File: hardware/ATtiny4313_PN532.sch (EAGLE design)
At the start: 21 parts, among them IC1 ATtiny4313, J2 AVR ISP, U1 PCA9543AD,118, U3 LTC490CN8PBF, U4 LTC490CN8PBF

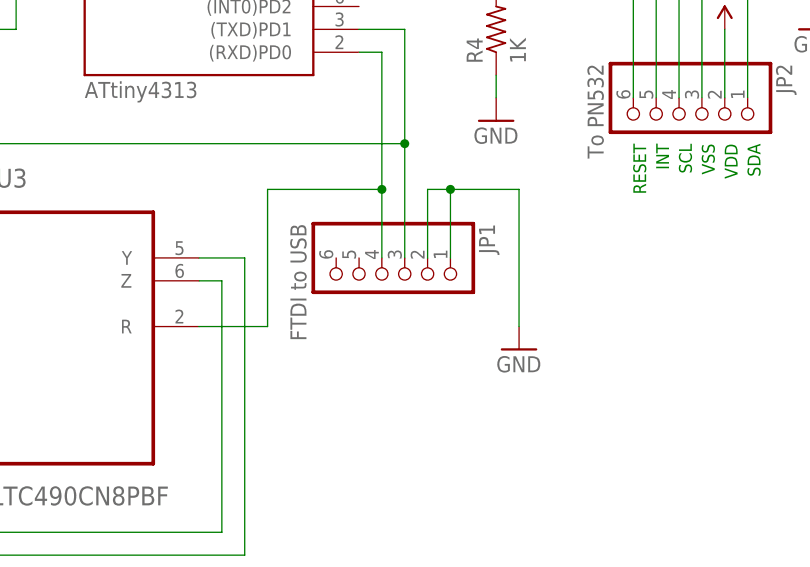
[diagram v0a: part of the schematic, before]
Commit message: Added I2C interface board (for prototypes)
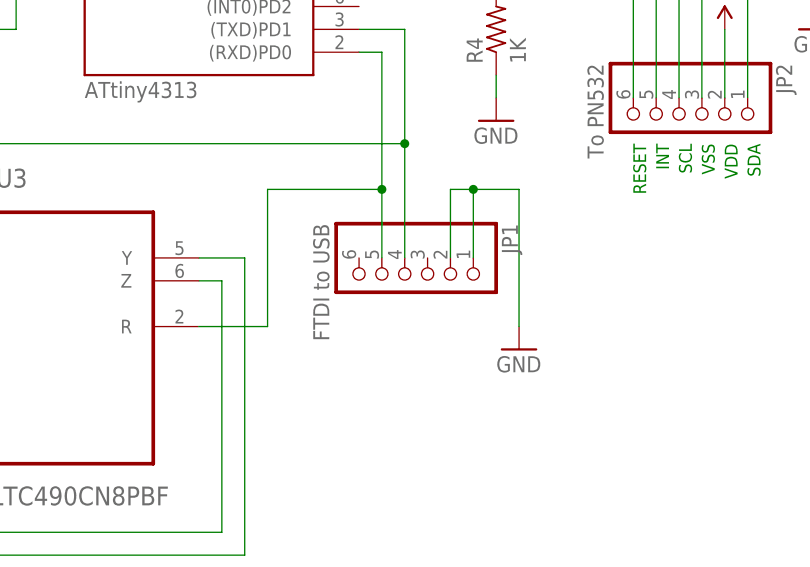
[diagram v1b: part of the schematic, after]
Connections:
- net N$3: now also JP1.4; no longer JP1.3
- net N$4: now also JP1.5; no longer JP1.4
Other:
- moved on the sheet: JP1
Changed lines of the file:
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@@
 <instance part="P+2" gate="1" x="203.2" y="175.26"/>
 <instance part="J2" gate="G$1" x="86.36" y="162.56"/>
-<instance part="JP1" gate="A" x="106.68" y="81.28" rot="R270"/>
+<instance part="JP1" gate="A" x="109.22" y="81.28" rot="R270"/>
 <instance part="GND3" gate="1" x="121.92" y="73.66"/>
 <instance part="LED1" gate="G$1" x="119.38" y="121.92"/>
@@
 <wire x1="121.92" y1="91.44" x2="121.92" y2="76.2" width="0.1524" layer="91"/>
 <pinref part="JP1" gate="A" pin="2"/>
-<wire x1="111.76" y1="83.82" x2="111.76" y2="91.44" width="0.1524" layer="91"/>
-<wire x1="111.76" y1="91.44" x2="114.3" y2="91.44" width="0.1524" layer="91"/>
+<wire x1="114.3" y1="83.82" x2="114.3" y2="91.44" width="0.1524" layer="91"/>
+<wire x1="114.3" y1="91.44" x2="116.84" y2="91.44" width="0.1524" layer="91"/>
 <pinref part="JP1" gate="A" pin="1"/>
-<wire x1="114.3" y1="91.44" x2="121.92" y2="91.44" width="0.1524" layer="91"/>
-<wire x1="114.3" y1="83.82" x2="114.3" y2="91.44" width="0.1524" layer="91"/>
-<junction x="114.3" y="91.44"/>
+<wire x1="116.84" y1="91.44" x2="121.92" y2="91.44" width="0.1524" layer="91"/>
+<wire x1="116.84" y1="83.82" x2="116.84" y2="91.44" width="0.1524" layer="91"/>
+<junction x="116.84" y="91.44"/>
 </segment>
 <segment>
@@
 <wire x1="104.14" y1="109.22" x2="109.22" y2="109.22" width="0.1524" layer="91"/>
 <wire x1="109.22" y1="109.22" x2="109.22" y2="96.52" width="0.1524" layer="91"/>
-<pinref part="JP1" gate="A" pin="3"/>
 <pinref part="U3" gate="A" pin="D"/>
-<wire x1="109.22" y1="96.52" x2="109.22" y2="83.82" width="0.1524" layer="91"/>
 <wire x1="50.8" y1="71.12" x2="45.72" y2="71.12" width="0.1524" layer="91"/>
 <wire x1="45.72" y1="71.12" x2="45.72" y2="96.52" width="0.1524" layer="91"/>
 <wire x1="45.72" y1="96.52" x2="109.22" y2="96.52" width="0.1524" layer="91"/>
+<pinref part="JP1" gate="A" pin="4"/>
+<wire x1="109.22" y1="96.52" x2="109.22" y2="83.82" width="0.1524" layer="91"/>
 <junction x="109.22" y="96.52"/>
 </segment>
@@
 <segment>
 <pinref part="IC1" gate="G$1" pin="(RXD)PD0"/>
-<pinref part="JP1" gate="A" pin="4"/>
 <wire x1="104.14" y1="106.68" x2="106.68" y2="106.68" width="0.1524" layer="91"/>
 <wire x1="106.68" y1="106.68" x2="106.68" y2="91.44" width="0.1524" layer="91"/>
 <pinref part="U3" gate="A" pin="R"/>
-<wire x1="106.68" y1="91.44" x2="106.68" y2="83.82" width="0.1524" layer="91"/>
 <wire x1="86.36" y1="76.2" x2="93.98" y2="76.2" width="0.1524" layer="91"/>
 <wire x1="93.98" y1="76.2" x2="93.98" y2="91.44" width="0.1524" layer="91"/>
 <wire x1="93.98" y1="91.44" x2="106.68" y2="91.44" width="0.1524" layer="91"/>
+<pinref part="JP1" gate="A" pin="5"/>
+<wire x1="106.68" y1="91.44" x2="106.68" y2="83.82" width="0.1524" layer="91"/>
 <junction x="106.68" y="91.44"/>
 </segment>

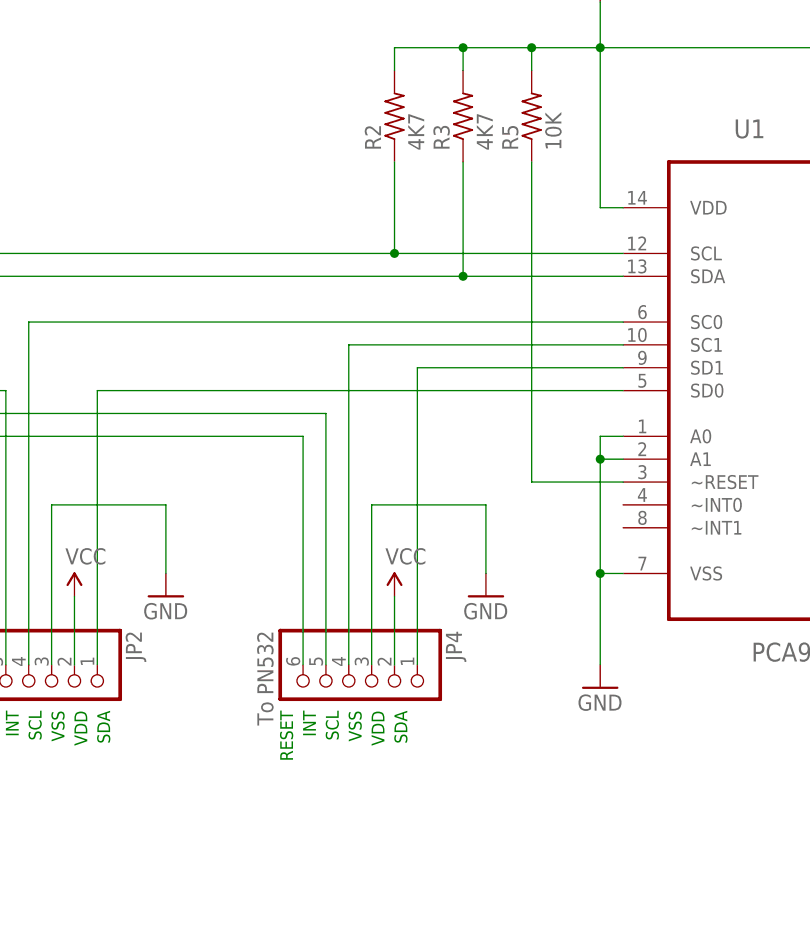
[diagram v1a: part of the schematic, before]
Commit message: Connected PCA9543 to reset to match the hardware
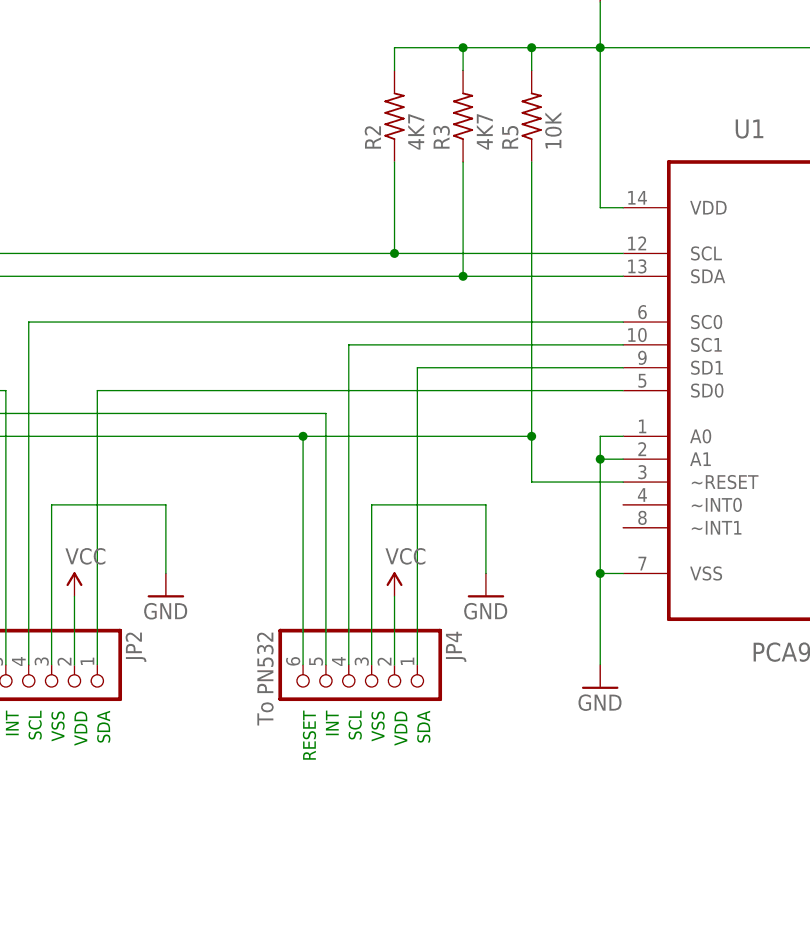
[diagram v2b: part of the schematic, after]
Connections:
- removed net N$15: R5.1, U1.~RESET
- net N$14: now also R5.1, U1.~RESET
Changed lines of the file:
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@@
 <setting verticaltext="up"/>
 </settings>
-<grid distance="0.1" unitdist="inch" unit="inch" style="lines" multiple="1" display="yes" altdistance="0.01" altunitdist="inch" altunit="inch"/>
+<grid distance="0.1" unitdist="inch" unit="inch" style="lines" multiple="1" display="no" altdistance="0.01" altunitdist="inch" altunit="inch"/>
 <layers>
 <layer number="1" name="Top" color="4" fill="1" visible="no" active="no"/>
@@
 <text x="137.16" y="96.52" size="1.4224" layer="91" rot="R270">INT</text>
 <text x="134.62" y="96.52" size="1.4224" layer="91" rot="R270">RESET</text>
-<text x="180.34" y="96.52" size="1.4224" layer="91" rot="R270">SDA</text>
-<text x="177.8" y="96.52" size="1.4224" layer="91" rot="R270">VDD</text>
-<text x="175.26" y="96.52" size="1.4224" layer="91" rot="R270">VSS</text>
-<text x="172.72" y="96.52" size="1.4224" layer="91" rot="R270">SCL</text>
-<text x="170.18" y="96.52" size="1.4224" layer="91" rot="R270">INT</text>
-<text x="167.64" y="96.52" size="1.4224" layer="91" rot="R270">RESET</text>
+<text x="182.88" y="96.52" size="1.4224" layer="91" rot="R270">SDA</text>
+<text x="180.34" y="96.52" size="1.4224" layer="91" rot="R270">VDD</text>
+<text x="177.8" y="96.52" size="1.4224" layer="91" rot="R270">VSS</text>
+<text x="175.26" y="96.52" size="1.4224" layer="91" rot="R270">SCL</text>
+<text x="172.72" y="96.52" size="1.4224" layer="91" rot="R270">INT</text>
+<text x="170.18" y="96.52" size="1.4224" layer="91" rot="R270">RESET</text>
 </plain>
 <instances>
@@
 <pinref part="JP2" gate="A" pin="6"/>
 <pinref part="JP4" gate="A" pin="6"/>
-</segment>
-</net>
-<net name="N$15" class="0">
-<segment>
 <pinref part="U1" gate="A" pin="~RESET"/>
-<wire x1="195.58" y1="157.48" x2="195.58" y2="121.92" width="0.1524" layer="91"/>
+<wire x1="195.58" y1="157.48" x2="195.58" y2="127" width="0.1524" layer="91"/>
+<wire x1="195.58" y1="127" x2="195.58" y2="121.92" width="0.1524" layer="91"/>
 <wire x1="195.58" y1="121.92" x2="205.74" y2="121.92" width="0.1524" layer="91"/>
 <pinref part="R5" gate="G$1" pin="1"/>
-</segment>
-</net>
+<wire x1="170.18" y1="127" x2="195.58" y2="127" width="0.1524" layer="91"/>
+<junction x="170.18" y="127"/>
+<junction x="195.58" y="127"/>
+</segment>
+</net>

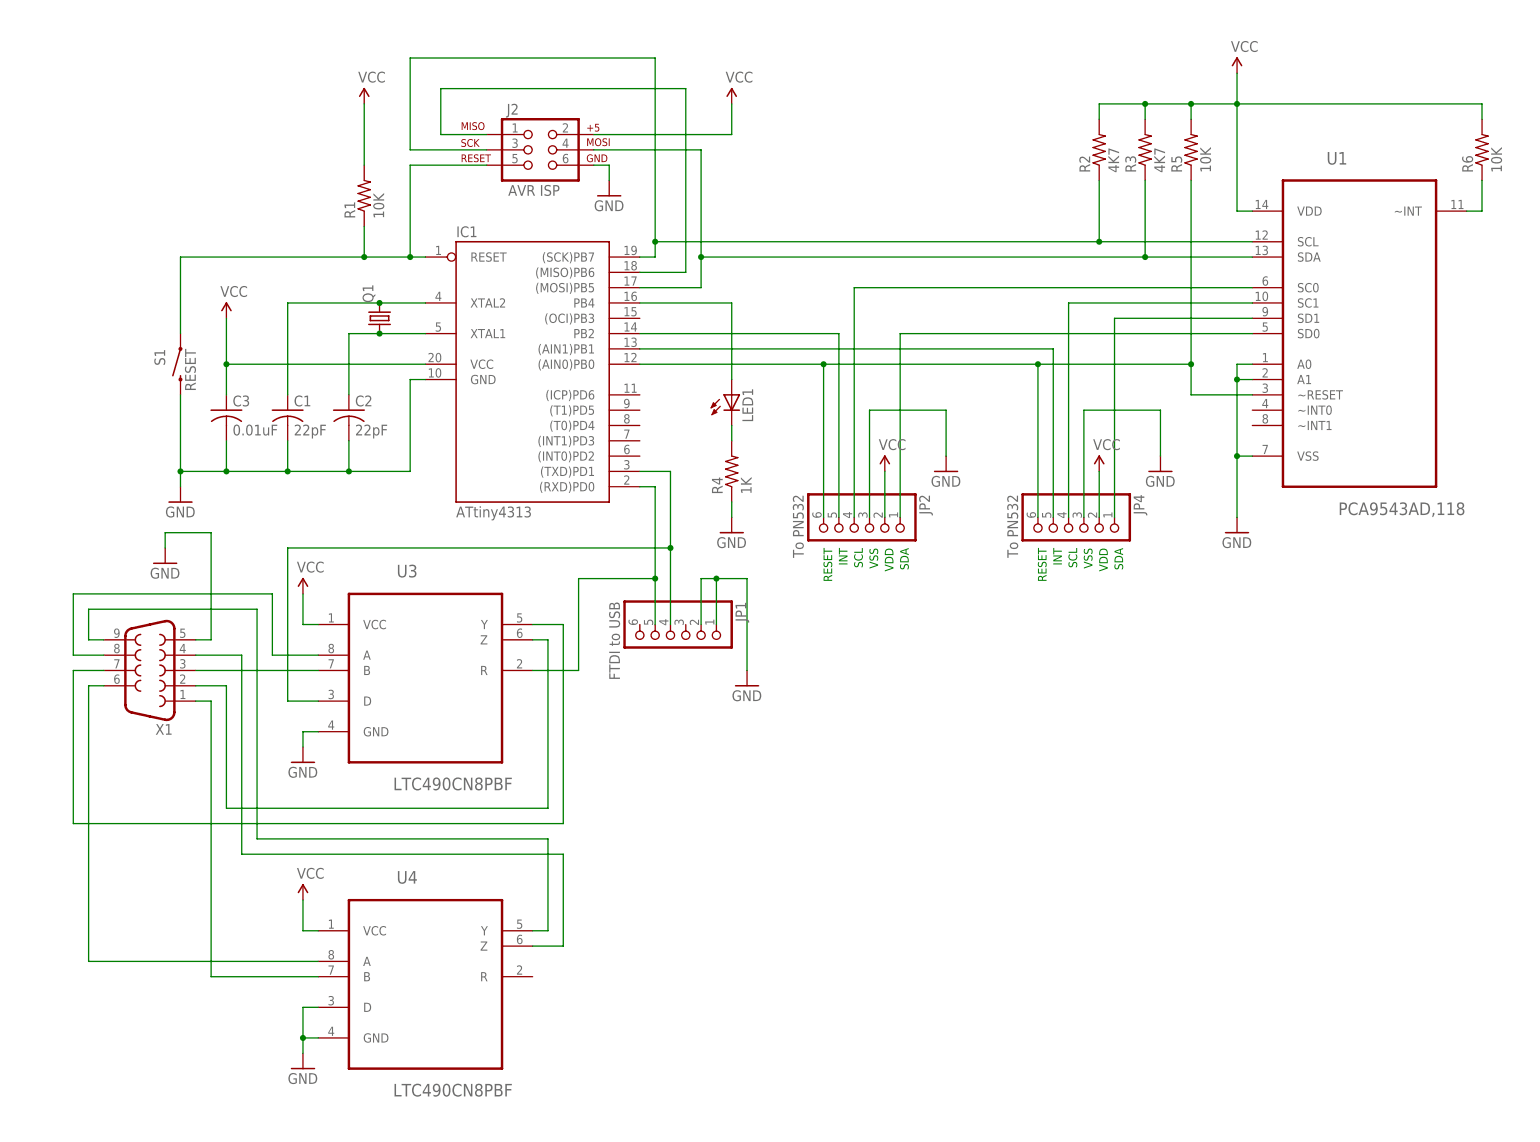
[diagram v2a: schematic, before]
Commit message: Corrected INT wiring
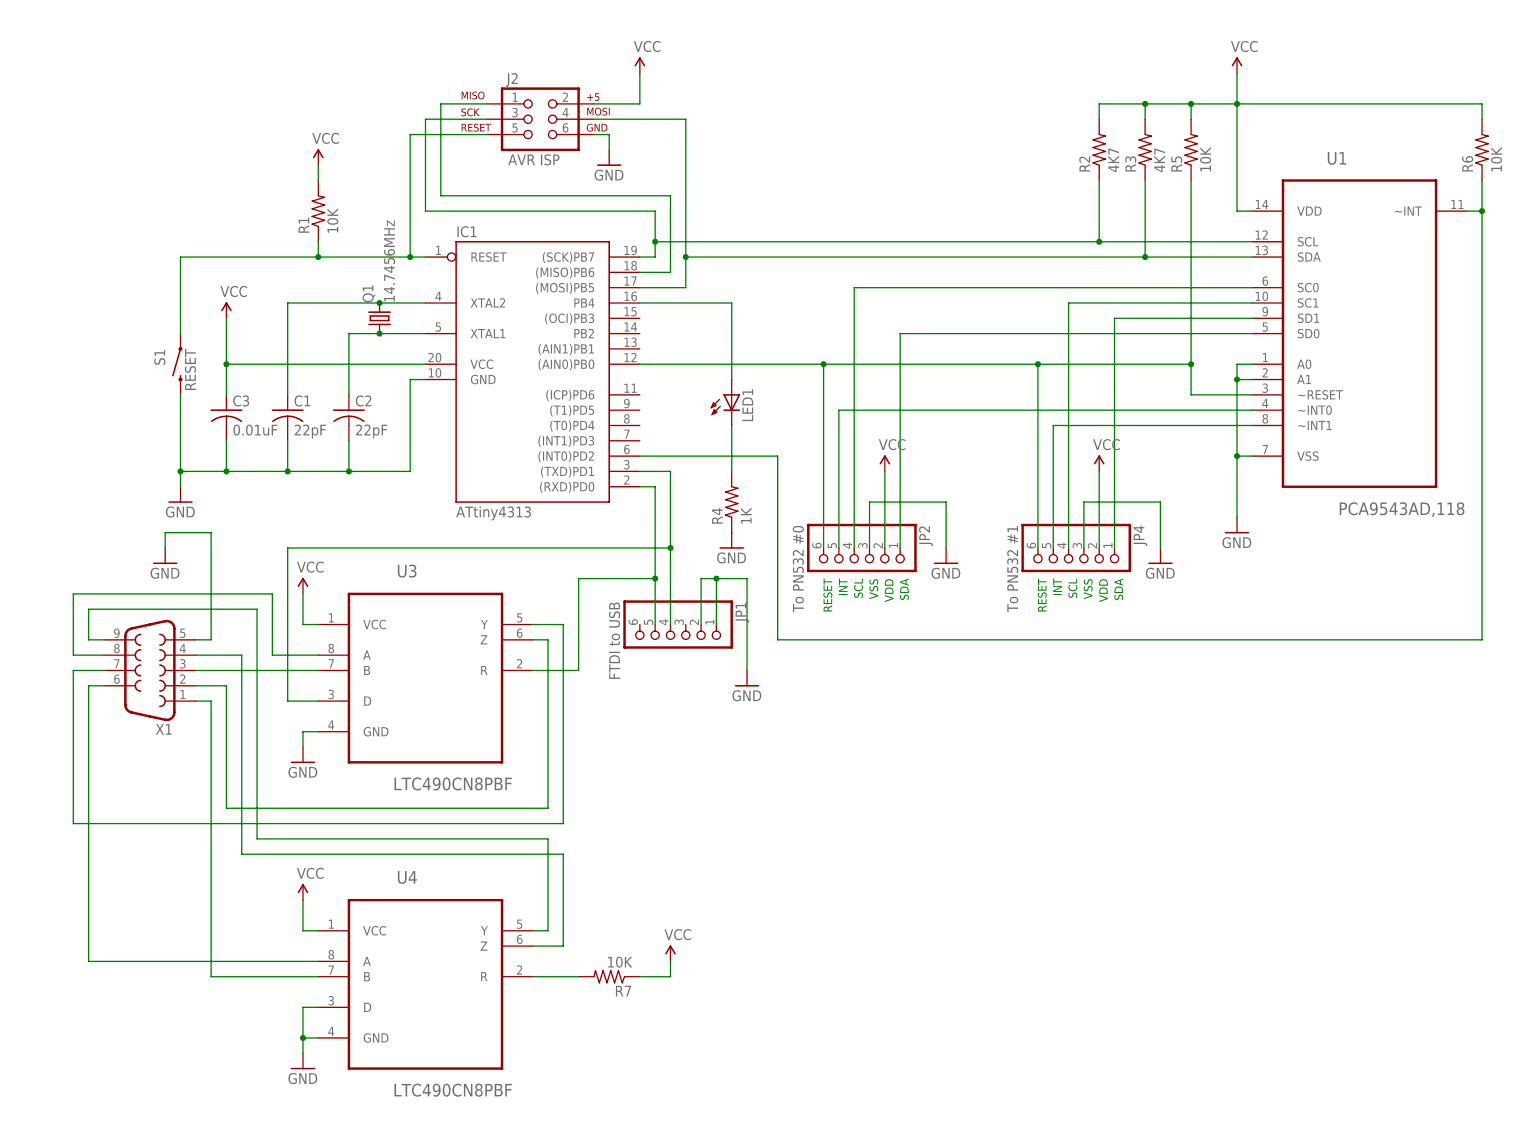
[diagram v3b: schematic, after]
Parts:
- added R7: 10K, rcl:R-US_0204/2V
- JP2: value To PN532 -> To PN532 #0
- JP4: value To PN532 -> To PN532 #1
- Q1: value (none) -> 14.7456MHz
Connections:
- removed net N$17: IC1.(AIN1)PB1, JP4.5
- new net N$18: JP4.5, U1.~INT1
- new net N$5: R7.2, U4.R
- net N$16: now also U1.~INT0; no longer IC1.PB2
- net N$8: now also IC1.(INT0)PD2
- net VCC: now also R7.1
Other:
- moved on the sheet: J2, JP2, JP4, R1, R4
